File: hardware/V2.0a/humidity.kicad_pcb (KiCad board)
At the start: 2 copper layers, 15 x 25 mm, 24 parts, among them P101 CON-SENSOR2, P102 BOOT, P103 DEBUG, U101 XMC1XXX24, U102 SHT3x-DIS, U103 DRILL, U104 DRILL, U105 DRILL, U106 DRILL

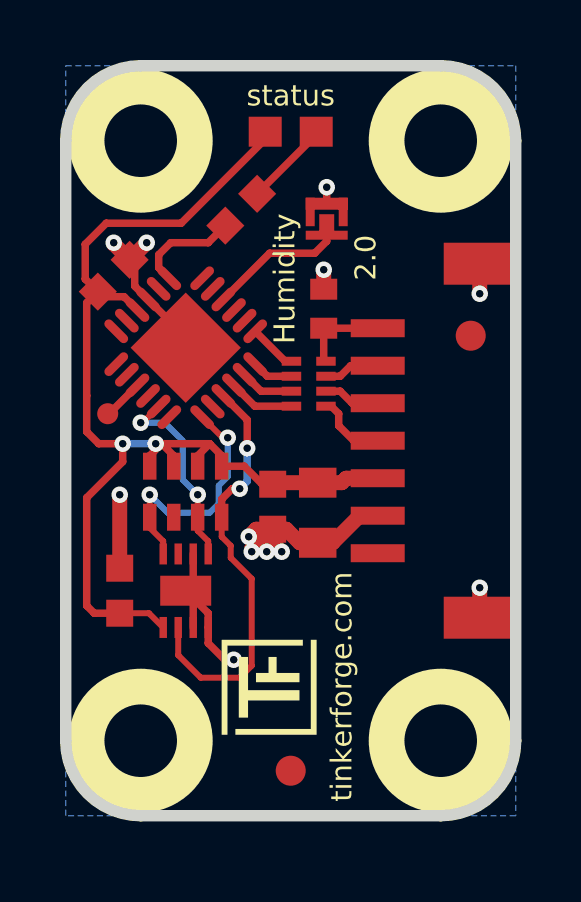
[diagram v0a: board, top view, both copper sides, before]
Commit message: add second prototype (alternative)
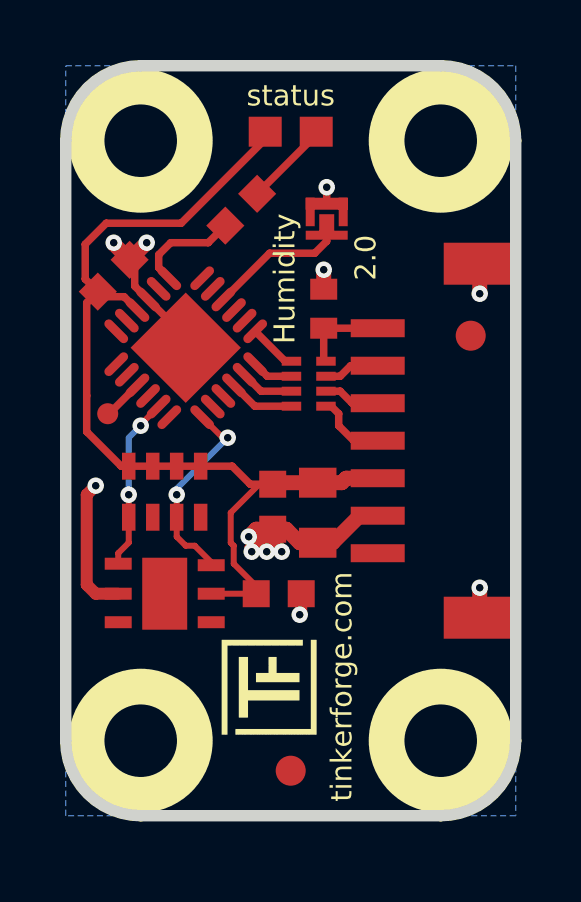
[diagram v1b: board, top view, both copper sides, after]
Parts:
- P102: value BOOT -> DEBUG; footprint kicad-libraries:SolderJumper -> kicad-libraries:DEBUG_PAD
- P103: value DEBUG -> BOOT; footprint kicad-libraries:DEBUG_PAD -> kicad-libraries:SolderJumper
- U102: value SHT3x-DIS -> HDC1080; footprint kicad-libraries:DFN8-25x25 -> kicad-libraries:DFN6-30x30
- moved P102 9.77 mm to (141.5, 140.1)
- moved P103 9.77 mm to (148.8, 133.6), turned to 270 degrees
- moved C105 5.30 mm to (147.2, 146.1), turned to 0 degrees
- moved U102 0.71 mm to (143.4, 146.1), turned to 90 degrees
- moved RP102 0.70 mm to (143.4, 142.7)
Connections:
- P102 pad 1: GND -> Net-(P102-Pad1)
- P103 pad 1: Net-(P103-Pad1) -> GND
- RP102 pad 5: SCL -> SDA
- RP102 pad 7: SDA -> SCL
- RP102 pad 8: nRESET -> (no net)
- U101 pad 15: Net-(P103-Pad1) -> Net-(P102-Pad1)
- U101 pad 21: nRESET -> (no net)
- U101 pad 4: Net-(P102-Pad2) -> Net-(P103-Pad2)
- U102 pad 4: SCL -> (no net)
- U102 pad 6: nRESET -> SCL
- U102 pad EXP: GND -> (no net)
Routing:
- net nRESET: track 14.1 -> 0.00 mm, vias 2 -> 0
- net VCC: track 38.1 -> 33.1 mm, vias 2 -> 0
- net Net-(P103-Pad2): track 0.00 -> 4.85 mm
- net Net-(P102-Pad2): track 4.85 -> 0.00 mm
- net GND: track 29.5 -> 26.6 mm
- net SCL: track 8.29 -> 6.74 mm
- net Net-(P103-Pad1): track 1.38 -> 0.00 mm
- net Net-(P102-Pad1): track 0.00 -> 1.38 mm
- net SDA: track 6.60 -> 5.80 mm

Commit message: add description
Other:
- board text added: "Copyright Tinkerforge GmbH 2017. This documentation describes Open Hardware and is licensed under the CERN OHL v. 1.1. You may redistribute and modify this documentation under the terms of the CERN OHL v.1.1. (http://ohwr.org/cernohl). This documentation is distributed WITHOUT ANY EXPRESS OR IMPLIED WARRANTY, INCLUDING OF MERCHANTABILITY, SATISFACTORY QUALITY AND FITNESS FOR A PARTICULAR PURPOSE.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"
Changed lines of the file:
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@@
     (links 45)
     (no_connects 0)
-    (area 139.909499 128.309499 155.290501 153.690501)
+    (area 139.244999 127.644999 155.955001 154.355001)
     (thickness 1.6)
-    (drawings 12)
+    (drawings 13)
     (tracks 149)
     (zones 0)
@@
   )
   (page A4)
+  (title_block
+    (title "Humidity Bricklet")
+    (date 2017-05-08)
+    (rev 2.0)
+    (company "Tinkerforge GmbH")
+    (comment 1 "Licensed under CERN OHL v.1.1")
+    (comment 2 "Copyright (©) 2017, B.Nordmeyer <bastian@tinkerforge.com>")
+  )
   (layers
     (0 F.Cu signal)
@@
   )
   (setup
-    (last_trace_width 0.4)
+    (last_trace_width 0.2)
     (user_trace_width 0.25)
     (user_trace_width 0.3)
@@
     (pad EXP smd rect (at 0 0 90) (size 2.4 1.5) (layers F.Cu F.Paste F.Mask))
   )
+  (gr_text "Copyright Tinkerforge GmbH 2017.\nThis documentation describes Open Hardware and is licensed under the\nCERN OHL v. 1.1.\nYou may redistribute and modify this documentation under the terms of the\nCERN OHL v.1.1. (http://ohwr.org/cernohl). This documentation is distributed\nWITHOUT ANY EXPRESS OR IMPLIED WARRANTY, INCLUDING OF\nMERCHANTABILITY, SATISFACTORY QUALITY AND FITNESS FOR A\nPARTICULAR PURPOSE. Please see the CERN OHL v.1.1 for applicable\nconditions" (at 251.55 152) (layer Cmts.User)
+    (effects (font (size 0.8 0.8) (thickness 0.15)))
+  )
   (gr_text 2.0 (at 150.1 134.9 90) (layer F.SilkS)
